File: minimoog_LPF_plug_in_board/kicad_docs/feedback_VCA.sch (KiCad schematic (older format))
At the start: 17 parts, among them Q10 BCM847, Q11 MMBT3904, Q12 MMBT3904, Q13 MMBT3906, U1 TL072

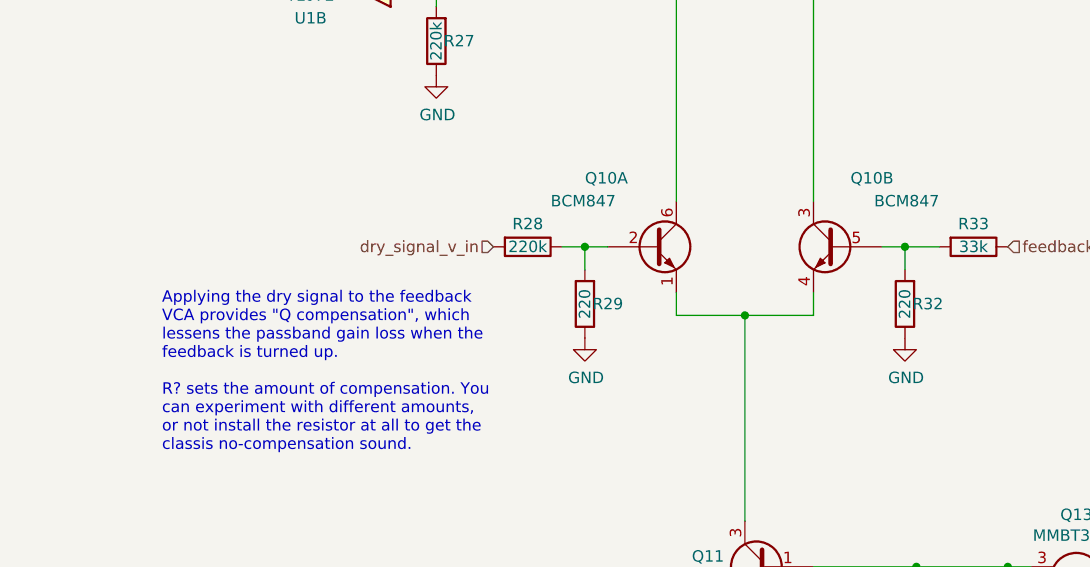
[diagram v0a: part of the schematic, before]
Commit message: add missing designator to schematic note
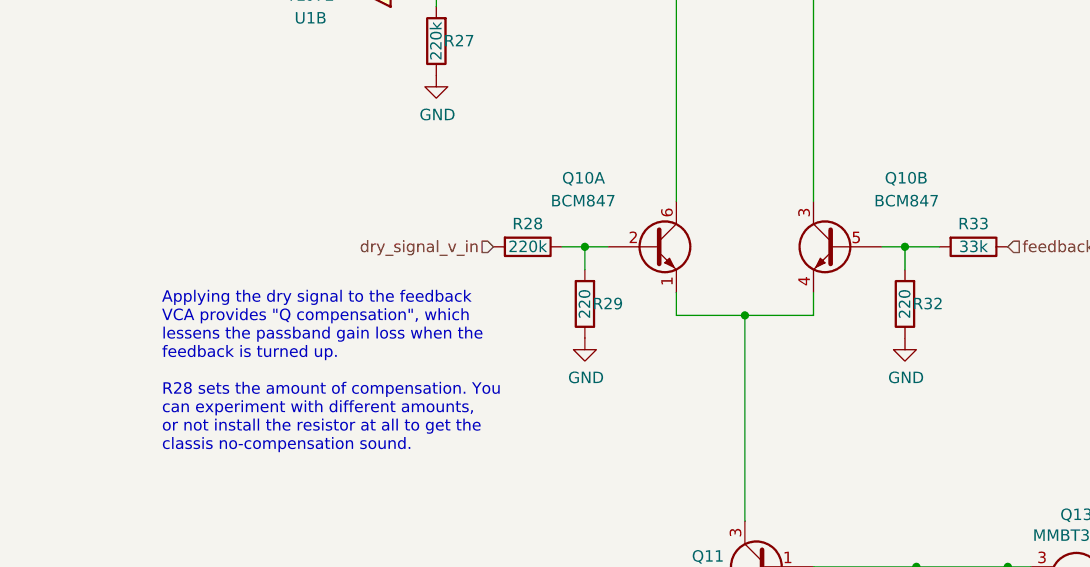
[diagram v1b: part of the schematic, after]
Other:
- note added: "Applying the dry signal to the feedback\nVCA provides "Q compensation", which\nlessens the passband gain loss when the\nfeedback is turned up.\n\nR28 sets the amount of compensation. You\ncan experiment with different amounts,\nor not install the resistor at all to get the \nclassis no-compensation sound.\n"
- note removed: "Applying the dry signal to the feedback\nVCA provides "Q compensation", which\nlessens the passband gain loss when the\nfeedback is turned up.\n\nR? sets the amount of compensation. You\ncan experiment with different amounts,\nor not install the resistor at all to get the \nclassis no-compensation sound.\n"
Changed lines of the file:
@@
 U 2 1 5F114A19
 P 5750 3550
-F 0 "Q10" H 5500 3850 50  0000 L CNN
+F 0 "Q10" H 5350 3850 50  0000 L CNN
 F 1 "BCM847" H 5300 3750 50  0000 L CNN
 F 2 "lpf_footprints:SOT457" H 5950 3475 50  0001 L CIN
@@
 U 1 1 5F12DDB3
 P 4950 3550
-F 0 "Q10" H 4650 3850 50  0000 L CNN
+F 0 "Q10" H 4550 3850 50  0000 L CNN
 F 1 "BCM847" H 4500 3750 50  0000 L CNN
 F 2 "lpf_footprints:SOT457" H 5150 3475 50  0001 L CIN
@@
 	4550 3550 4650 3550
 Text Notes 2800 4450 0    50   ~ 0
-Applying the dry signal to the feedback\nVCA provides "Q compensation", which\nlessens the passband gain loss when the\nfeedback is turned up.\n\nR? sets the amount of compensation. You\ncan experiment with different amounts,\nor not install the resistor at all to get the \nclassis no-compensation sound.\n
+Applying the dry signal to the feedback\nVCA provides "Q compensation", which\nlessens the passband gain loss when the\nfeedback is turned up.\n\nR28 sets the amount of compensation. You\ncan experiment with different amounts,\nor not install the resistor at all to get the \nclassis no-compensation sound.\n
 $Comp
 L Device:R R28
